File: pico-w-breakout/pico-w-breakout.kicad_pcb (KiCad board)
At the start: 2 copper layers, 44 x 59 mm, 8 parts, among them J1 Conn_01x20, J2 Conn_01x20, J3 Conn_01x20, J4 Conn_01x20, J5 Conn_01x03, J6 Conn_01x03

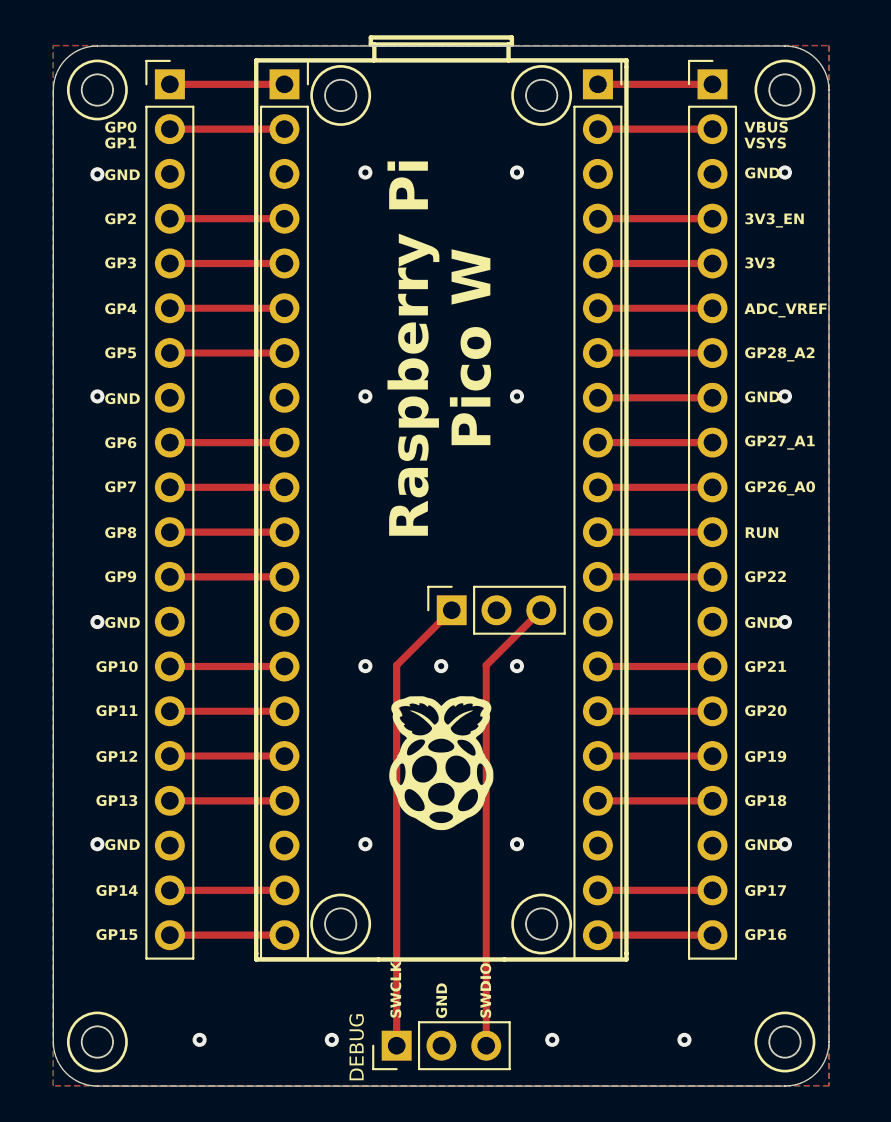
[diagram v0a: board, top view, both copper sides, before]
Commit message: Add series resistor to GPIO 2
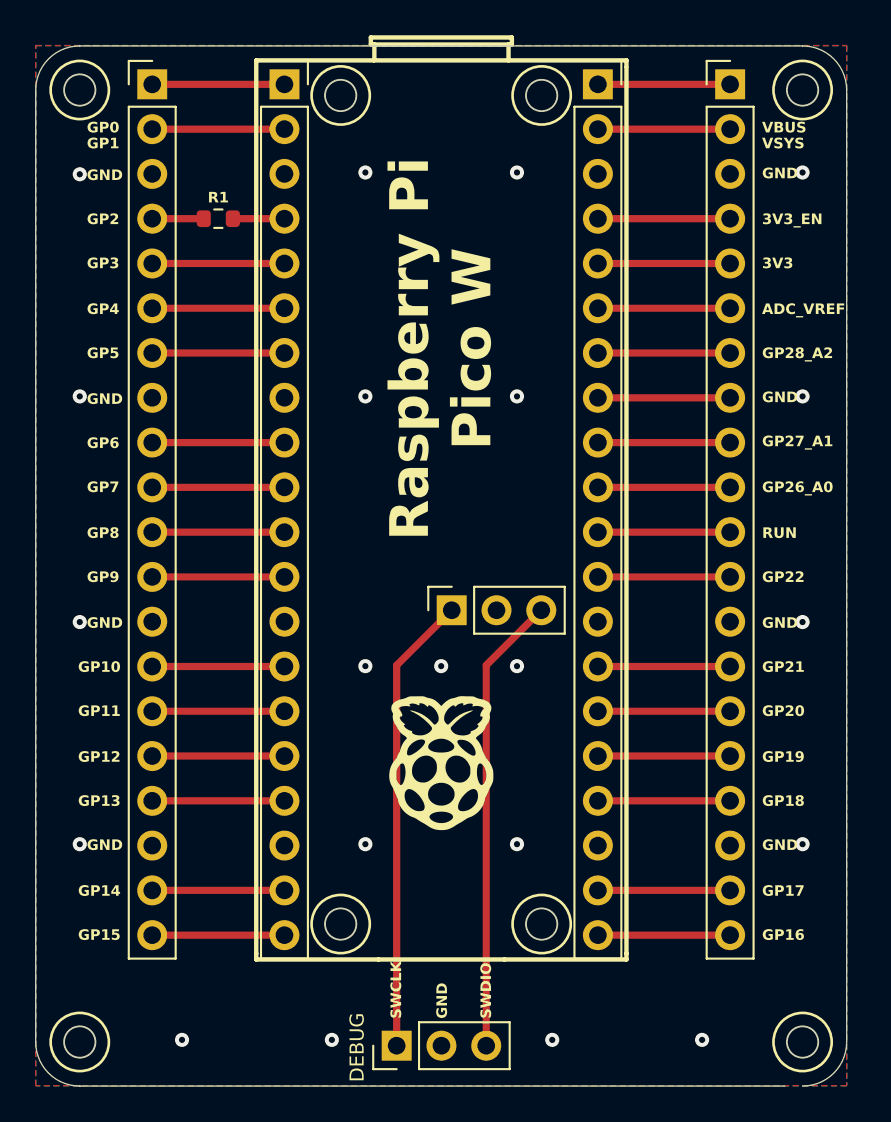
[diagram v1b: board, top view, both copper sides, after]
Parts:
- added R1: 10, Resistor_SMD:R_0603_1608Metric, F.Cu at (47.2, 47.7)
- moved J1 1.00 mm to (43.4, 40.1)
- moved J4 1.00 mm to (76.2, 40.1)
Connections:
- J2 pad 4: Net-(J1-Pin_4) -> Net-(J2-Pin_4)
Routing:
- net Net-(J1-Pin_4): track 6.50 -> 2.93 mm
- net Net-(J2-Pin_4): track 0.00 -> 2.92 mm
- net Net-(J3-Pin_9): track 6.50 -> 7.50 mm
- net Net-(J3-Pin_8): track 6.50 -> 7.50 mm
- net Net-(J3-Pin_7): track 6.50 -> 7.50 mm
- net Net-(J3-Pin_6): track 6.50 -> 7.50 mm
- net Net-(J3-Pin_5): track 6.50 -> 7.50 mm
- net Net-(J3-Pin_4): track 6.50 -> 7.50 mm
- net Net-(J3-Pin_20): track 6.50 -> 7.50 mm
- net Net-(J3-Pin_2): track 6.50 -> 7.50 mm
- net Net-(J3-Pin_19): track 6.50 -> 7.50 mm
- net Net-(J3-Pin_17): track 6.50 -> 7.50 mm
- net Net-(J3-Pin_16): track 6.50 -> 7.50 mm
- net Net-(J3-Pin_15): track 6.50 -> 7.50 mm
- net Net-(J3-Pin_14): track 6.50 -> 7.50 mm
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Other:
- board size 44 x 59 mm -> 46 x 59 mm

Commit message: Final update to Pico breakout boards
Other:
- outline, holes or cut-outs redrawn
- board text added: "AGND"
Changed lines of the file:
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@@
 	(footprint "Connector_PinSocket_2.54mm:PinSocket_1x03_P2.54mm_Vertical"
 		(layer "F.Cu")
-		(at 60.3991 69.93 90)
+		(at 60.3991 69.905 90)
 		(descr "Through hole straight socket strip, 1x03, 2.54mm pitch, single row (from Kicad 4.0.7), script generated")
 		(tags "Through hole socket strip THT 1x03 2.54mm single row")
@@
 	(gr_line
 		(start 39.3 96.921)
-		(end 79.3 96.921)
+		(end 80.3 96.921)
 		(stroke
 			(width 0.05)
@@
 		)
 	)
-	(gr_text "GND"
-		(at 73.4 58.2 0)
+	(gr_text "AGND"
+		(at 73.7 58.2 0)
 		(layer "B.SilkS")
 		(effects
@@
 		)
 	)
-	(gr_text "GND"
+	(gr_text "AGND"
 		(at 78 58.2 0)
 		(layer "F.SilkS")
@@
 	)
 	(segment
-		(start 62.355 94.63)
-		(end 62.355 73.0541)
+		(start 62.355 73.0291)
+		(end 65.4791 69.905)
 		(width 0.4064)
 		(layer "F.Cu")
@@
 	)
 	(segment
-		(start 62.355 73.0541)
-		(end 65.4791 69.93)
+		(start 62.355 94.63)
+		(end 62.355 73.0291)
 		(width 0.4064)
 		(layer "F.Cu")
@@
 	)
 	(segment
-		(start 57.275 94.63)
-		(end 57.275 73.0541)
+		(start 57.275 73.0291)
+		(end 60.3991 69.905)
 		(width 0.4064)
 		(layer "F.Cu")
@@
 	)
 	(segment
-		(start 57.275 73.0541)
-		(end 60.3991 69.93)
+		(start 57.275 94.63)
+		(end 57.275 73.0291)
 		(width 0.4064)
 		(layer "F.Cu")
